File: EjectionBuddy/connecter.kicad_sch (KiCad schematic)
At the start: 13 parts, among them J10 Conn_01x04, J11 Conn_01x04, J12 Conn_01x04, J13 Conn_01x04, J14 Conn_01x02, J3 Conn_01x04, J4 Conn_01x08, J5 Conn_01x04, J6 Conn_01x04, J7 Conn_01x04, J8 Conn_01x04, J9 Conn_01x04

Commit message: Finished! QR and instruction pending
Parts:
- added J14: Conn_01x08, Connector_JST:JST_GH_SM08B-GHS-TB_1x08-1MP_P1.25mm_Horizontal, symbol Connector_Generic:Conn_01x08
- D9: footprint (none) -> Diode_SMD:D_SOD-523
- J10: renamed from J3; footprint (none) -> Connector_JST:JST_GH_SM04B-GHS-TB_1x04-1MP_P1.25mm_Horizontal
- J11: renamed from J14; footprint (none) -> Connector_JST:JST_GH_SM02B-GHS-TB_1x02-1MP_P1.25mm_Horizontal
- J12: renamed from J11; footprint (none) -> Connector_JST:JST_GH_SM04B-GHS-TB_1x04-1MP_P1.25mm_Horizontal
- J13: renamed from J12; footprint (none) -> Connector_JST:JST_GH_SM04B-GHS-TB_1x04-1MP_P1.25mm_Horizontal
- J2: renamed from J5; footprint (none) -> Connector_JST:JST_GH_SM04B-GHS-TB_1x04-1MP_P1.25mm_Horizontal
- J3: renamed from J6; footprint (none) -> Connector_JST:JST_GH_SM04B-GHS-TB_1x04-1MP_P1.25mm_Horizontal
- J4: renamed from J7; footprint (none) -> Connector_JST:JST_GH_SM04B-GHS-TB_1x04-1MP_P1.25mm_Horizontal
- J5: renamed from J8; footprint (none) -> Connector_JST:JST_GH_SM04B-GHS-TB_1x04-1MP_P1.25mm_Horizontal
- J6: renamed from J4; footprint (none) -> Connector_JST:JST_GH_SM08B-GHS-TB_1x08-1MP_P1.25mm_Horizontal
- J7: renamed from J9; footprint (none) -> Connector_JST:JST_GH_SM04B-GHS-TB_1x04-1MP_P1.25mm_Horizontal
- J8: renamed from J10; footprint (none) -> Connector_JST:JST_GH_SM04B-GHS-TB_1x04-1MP_P1.25mm_Horizontal
- J9: renamed from J13; footprint (none) -> Connector_JST:JST_GH_SM04B-GHS-TB_1x04-1MP_P1.25mm_Horizontal
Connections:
- net +5C: now also J14.1 (Pin_1)
- net CAM_PWM_1: now also J12.2 (Pin_2); no longer J12.3 (Pin_3)
- net CAM_PWM_2: now also J13.2 (Pin_2); no longer J13.3 (Pin_3)
- net GND: now also J14.4 (Pin_4), J14.8 (Pin_8)
- new net SM.CLK: J14.7 (Pin_7)
- new net SM.DIO: J14.6 (Pin_6)
- new net SM.RX: J14.3 (Pin_3)
- new net SM.TX: J14.2 (Pin_2)
- no-connect marks 3 -> 4
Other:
- note added: "Battery port"
- note added: "Pull high to cut"
- note added: "Side-mcu programming port"
- note added: "V_{bat} output port"
- note removed: "Power port"
- note removed: "Simple Vbat output port"
- moved on the sheet: J11

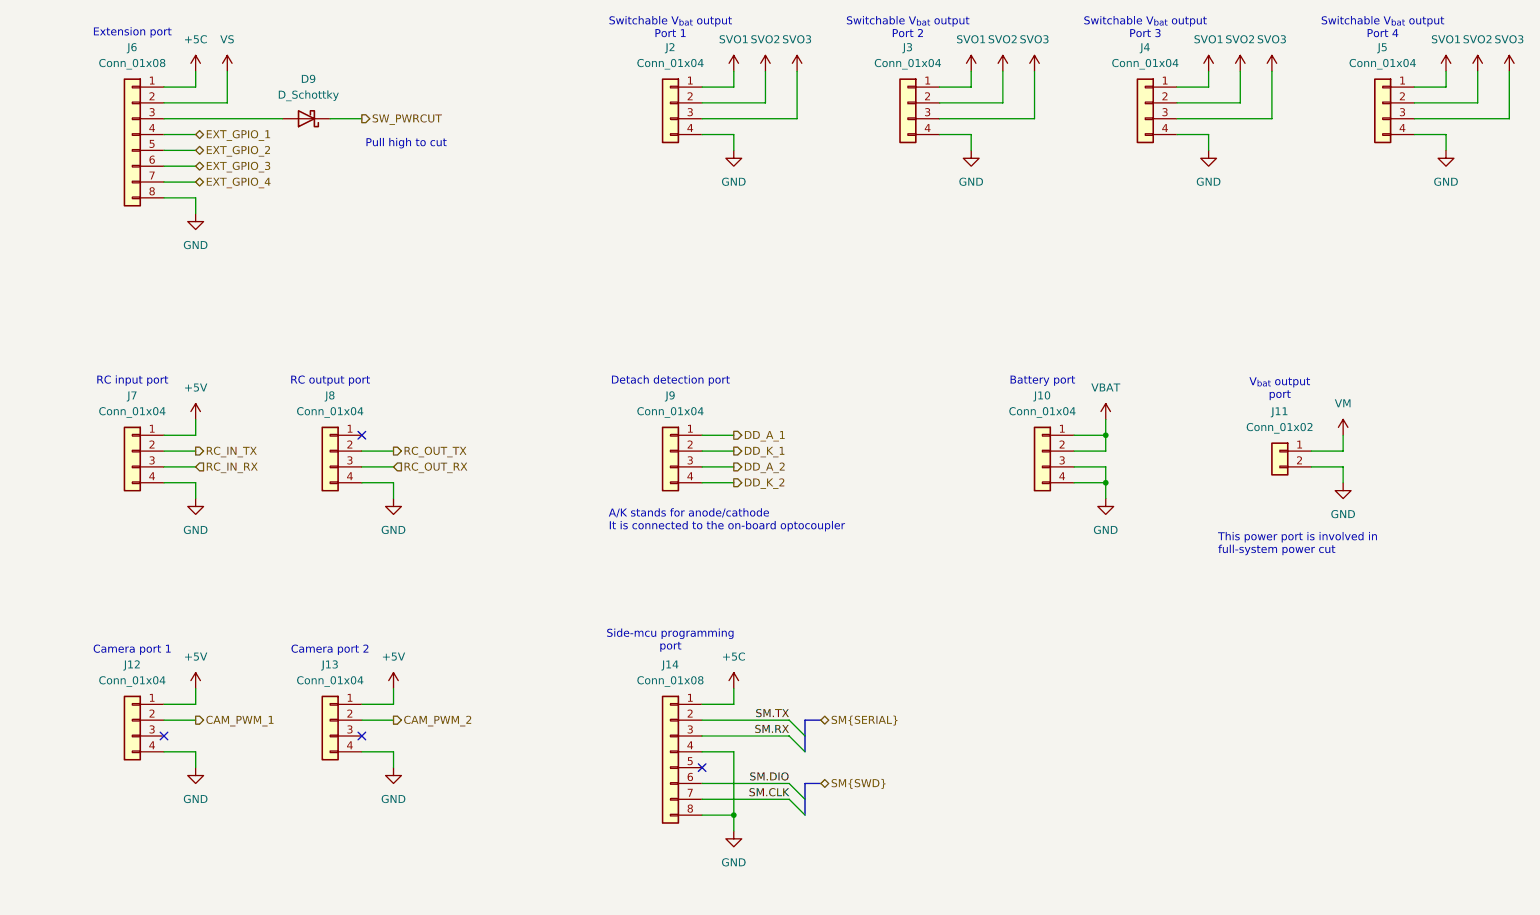
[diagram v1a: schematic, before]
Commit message: Side-mcu stm -> attiny, with improvements here and there
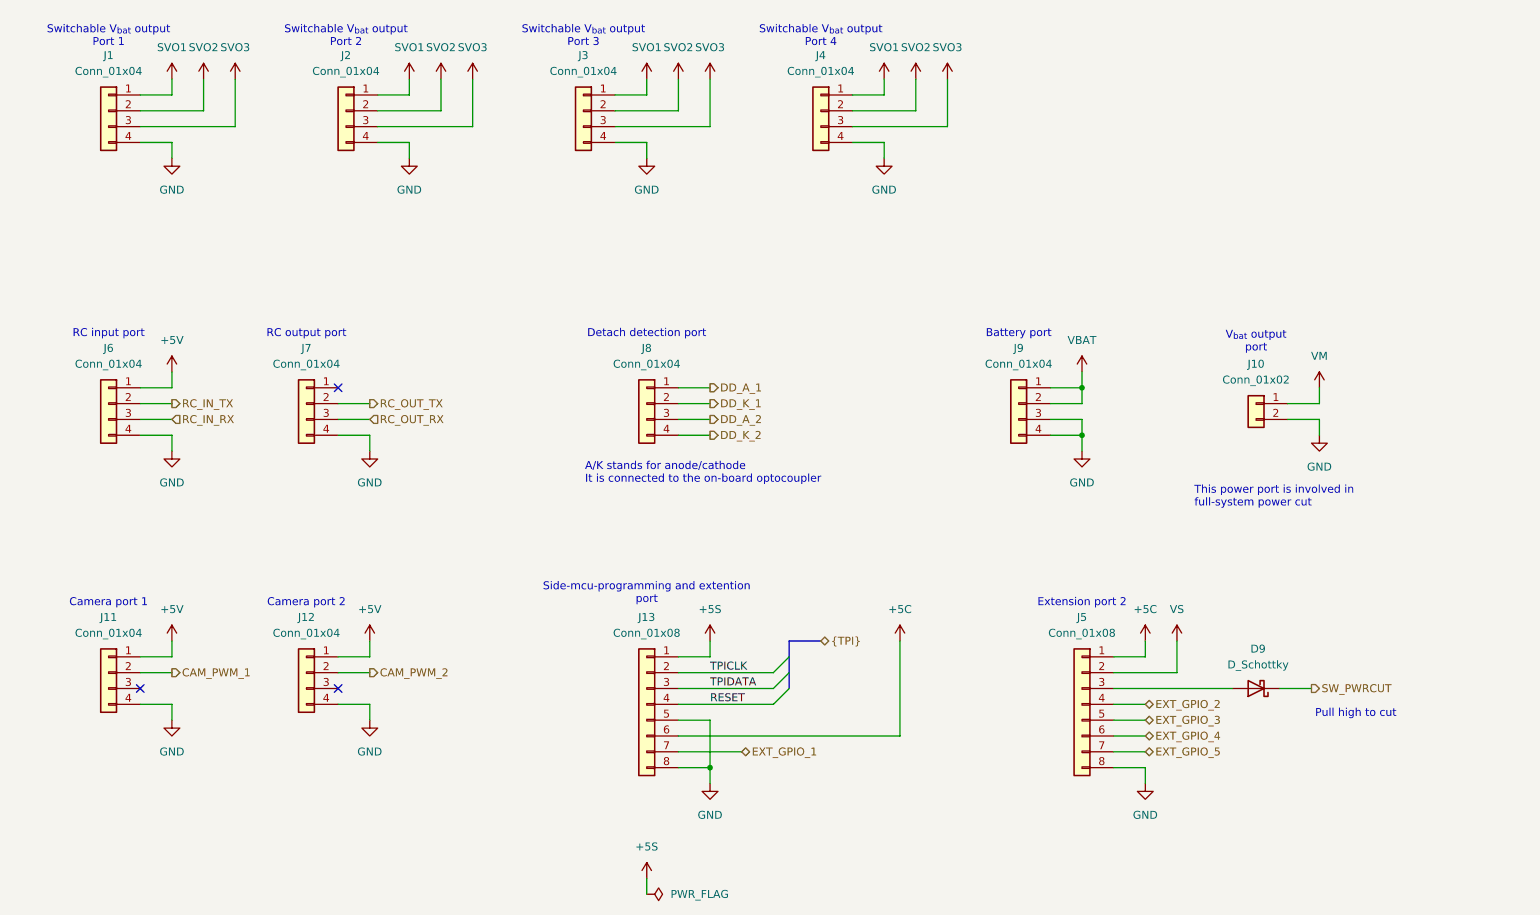
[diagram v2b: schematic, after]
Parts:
- removed J14: Conn_01x08, Connector_JST:JST_GH_SM08B-GHS-TB_1x08-1MP_P1.25mm_Horizontal, symbol Connector_Generic:Conn_01x08
- added J13: Conn_01x08, symbol Connector_Generic:Conn_01x08
- renumbered J2 to J1, J11 to J10, J12 to J11, J13 to J12, J3 to J2, J4 to J3, J5 to J4, J6 to J5, J7 to J6, J8 to J7, J9 to J8, J10 to J9
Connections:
- net +5C: now also J13.6 (Pin_6)
- net EXT_GPIO_1: now also J13.7 (Pin_7); no longer J5.4 (Pin_4)
- net EXT_GPIO_2: now also J5.4 (Pin_4); no longer J5.5 (Pin_5)
- net EXT_GPIO_3: now also J5.5 (Pin_5); no longer J5.6 (Pin_6)
- net EXT_GPIO_4: now also J5.6 (Pin_6); no longer J5.7 (Pin_7)
- net GND: now also J13.5 (Pin_5), J13.8 (Pin_8)
- new net +5S: J13.1 (Pin_1)
- new net EXT_GPIO_5: J5.7 (Pin_7)
- new net RESET: J13.4 (Pin_4)
- new net TPICLK: J13.2 (Pin_2)
- new net TPIDATA: J13.3 (Pin_3)
- no-connect marks 4 -> 3
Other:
- note added: "Extension port 2"
- note added: "Side-mcu-programming and extention port"
- note removed: "Extension port"
- note removed: "Side-mcu programming port"
- moved on the sheet: D9, J1, J10, J11, J12, J2, J3, J4, J5, J6, J7, J8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

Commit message: Prodection version hw1.0 finished, with tidy-ups and bug-fixes
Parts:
- J12: renamed from J13; footprint (none) -> Connector_JST:JST_GH_SM08B-GHS-TB_1x08-1MP_P1.25mm_Horizontal
- renumbered J11 to J10, J12 to J11, J5 to J13, J6 to J5, J7 to J6, J8 to J7, J9 to J8, J10 to J9

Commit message: Add Vbat voltage limit warning to schematic
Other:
- note added: "V_{bat} 30V max"
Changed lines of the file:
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@@
+		)
+	)
+	(text "V_{bat} 30V max"
+		(exclude_from_sim no)
+		(at 182.626 105.41 0)
+		(effects
+			(font
+				(size 1.27 1.27)
+			)
+			(justify left)
 		)
 	)
